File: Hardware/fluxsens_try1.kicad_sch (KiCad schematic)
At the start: 29 parts, among them J1 Conn_Coaxial, J2 Conn_Coaxial, J3 Conn_01x03, U1 DRV5033AJQDBZ, U3 DRV5033AJQDBZ, U5 DRV5033AJQDBZ, U6 DRV5033AJQDBZ

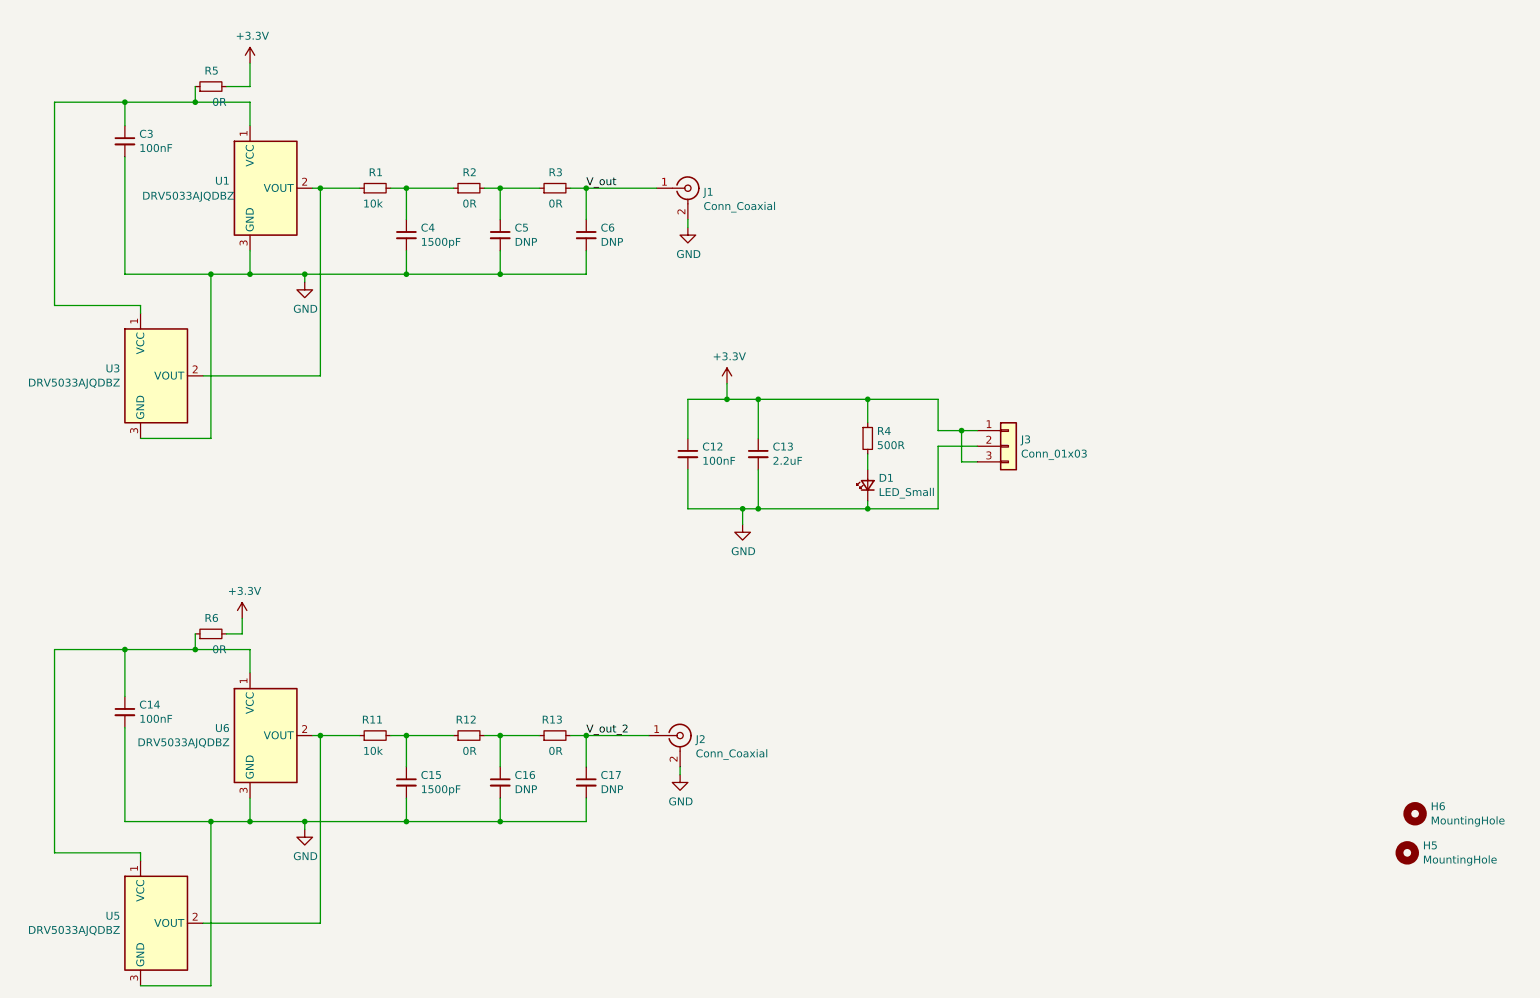
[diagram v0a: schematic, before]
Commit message: Update KiCad project files and add PCB markings
Updated .gitignore to exclude .zip files. Modified KiCad project, schematic, and settings files with new configuration and metadata. Added PCB markings image to Media directory. Lock files for KiCad PCB and schematic were added.
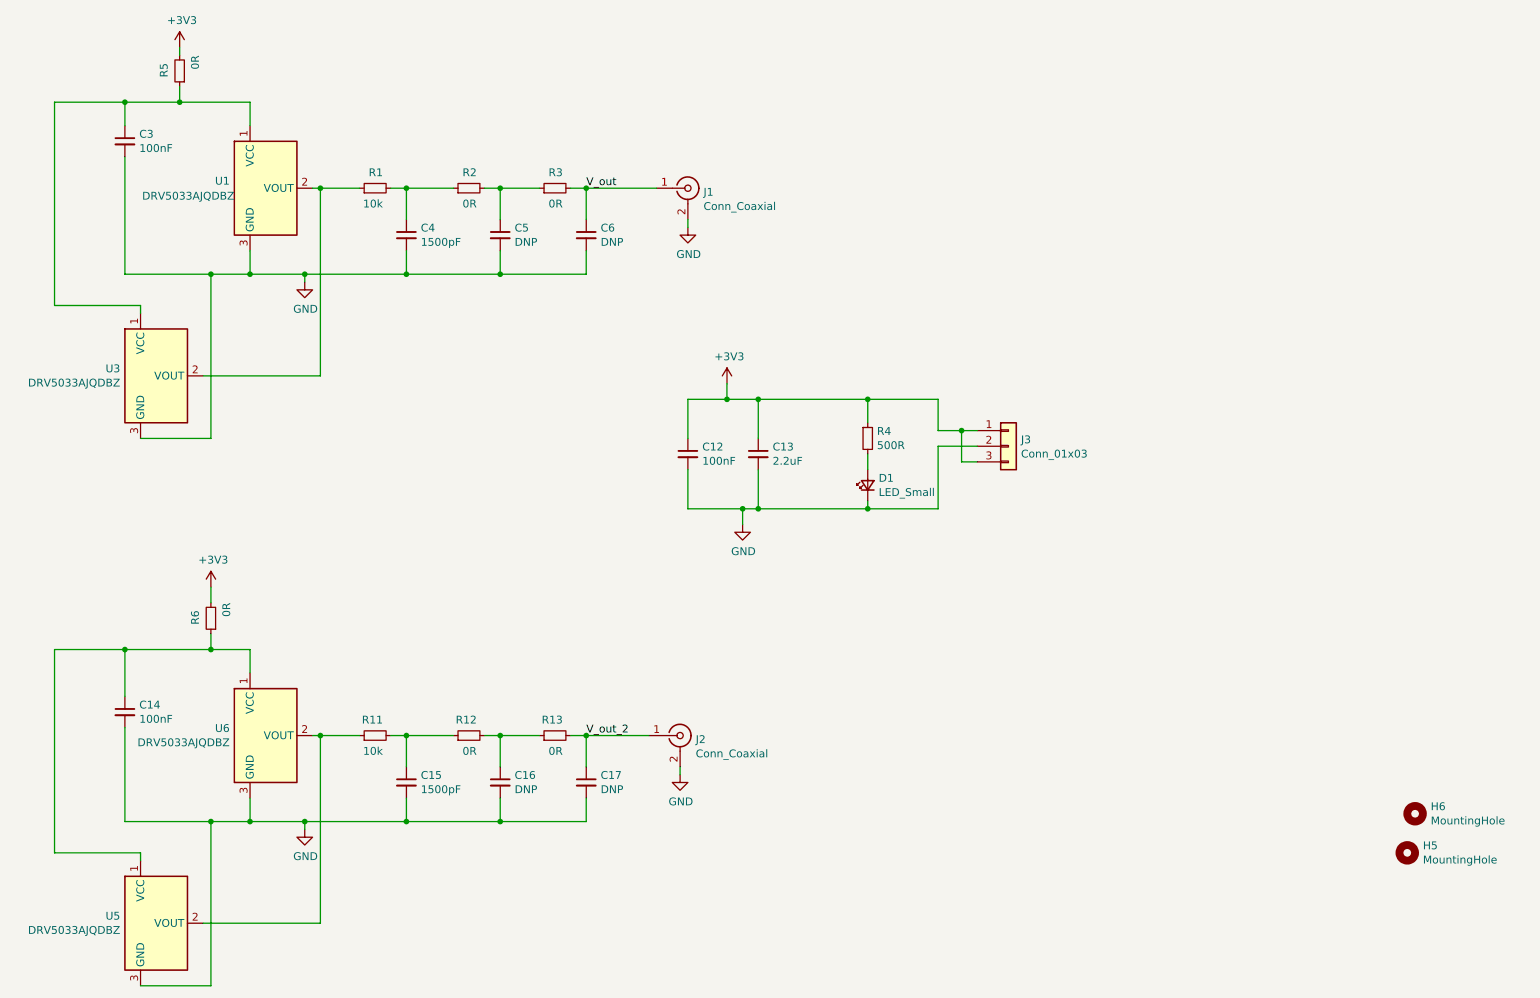
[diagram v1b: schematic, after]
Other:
- moved on the sheet: R5, R6
